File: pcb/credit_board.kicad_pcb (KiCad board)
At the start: 2 copper layers, 17 parts, among them J1 amp or pull-up, J2 amp or pull-up, J3 Jack-DC, J4 amp or pull-up, J5 clk, J6 clk, U1 74HC04, Y1 10MHz, Y2 32.768 kHz

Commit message: beta ground にした。
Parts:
- moved J3 9.24 mm to (171.8, 105.4)
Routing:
- net GND: track 60.3 -> 0.00 mm, vias 2 -> 0
- net VCC: track 73.6 -> 81.6 mm
- net Net-(J2-Pad3): track 5.08 -> 2.54 mm
- added copper zone on B.Cu, net GND
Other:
- board outline added: 45.7 x 41.9 mm
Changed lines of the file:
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@@
     (links 31)
     (no_connects 0)
-    (area 138.725 98.684999 181.535001 136.690002)
+    (area 139.624999 96.444999 185.495001 138.505001)
     (thickness 1.6)
-    (drawings 0)
-    (tracks 63)
+    (drawings 4)
+    (tracks 52)
     (zones 0)
     (modules 17)
@@
   )
   (module Connectors:Barrel_Jack_CUI_PJ-102AH (layer F.Cu)
-    (at 162.56 105.41 90)
+    (at 171.8 105.41 90)
     (descr "Thin-pin DC Barrel Jack, https://cdn-shop.adafruit.com/datasheets/21mmdcjackDatasheet.pdf")
     (tags "Power Jack")
@@
     )
   )
+  (gr_line (start 185.42 138.43) (end 185.42 96.52) (layer Edge.Cuts) (width 0.15))
+  (gr_line (start 139.7 138.43) (end 185.42 138.43) (layer Edge.Cuts) (width 0.15))
+  (gr_line (start 139.7 96.52) (end 139.7 138.43) (layer Edge.Cuts) (width 0.15))
+  (gr_line (start 185.42 96.52) (end 139.7 96.52) (layer Edge.Cuts) (width 0.15))
   (segment (start 172.72 115.57) (end 170.18 115.57) (width 0.25) (layer B.Cu) (net 1))
   (segment (start 175.26 115.57) (end 172.72 115.57) (width 0.25) (layer B.Cu) (net 1))
@@
   (segment (start 170.18 115.57) (end 167.64 115.57) (width 0.25) (layer B.Cu) (net 1))
   (segment (start 162.74 115.75) (end 162.56 115.57) (width 0.25) (layer B.Cu) (net 1))
-  (segment (start 180.26 115.57) (end 180.26 112.95) (width 0.25) (layer B.Cu) (net 2))
-  (segment (start 180.26 112.95) (end 172.72 105.41) (width 0.25) (layer B.Cu) (net 2))
-  (segment (start 180.26 115.57) (end 180.26 120.65) (width 0.25) (layer B.Cu) (net 2))
-  (segment (start 168.56 105.41) (end 172.72 105.41) (width 0.25) (layer B.Cu) (net 2))
-  (segment (start 167.64 135.89) (end 180.26 123.27) (width 0.25) (layer B.Cu) (net 2))
-  (segment (start 180.26 120.65) (end 180.26 123.27) (width 0.25) (layer B.Cu) (net 2))
-  (via (at 157.48 130.81) (size 0.6) (drill 0.4) (layers F.Cu B.Cu) (net 2))
-  (segment (start 157.48 133.35) (end 157.48 130.81) (width 0.25) (layer F.Cu) (net 2))
-  (segment (start 160.02 135.89) (end 157.48 133.35) (width 0.25) (layer F.Cu) (net 2))
-  (via (at 160.02 135.89) (size 0.6) (drill 0.4) (layers F.Cu B.Cu) (net 2))
-  (segment (start 154.94 128.27) (end 157.48 130.81) (width 0.25) (layer B.Cu) (net 2))
-  (segment (start 160.02 135.89) (end 167.64 135.89) (width 0.25) (layer B.Cu) (net 2))
   (segment (start 175.26 120.65) (end 174.134999 119.524999) (width 0.25) (layer B.Cu) (net 3))
   (segment (start 172.72 118.11) (end 175.26 120.65) (width 0.25) (layer B.Cu) (net 3))
@@
   (segment (start 165.1 125.73) (end 172.72 125.73) (width 0.25) (layer B.Cu) (net 8))
   (segment (start 165.1 125.73) (end 162.56 125.73) (width 0.25) (layer B.Cu) (net 8))
-  (segment (start 172.72 128.27) (end 167.64 128.27) (width 0.25) (layer B.Cu) (net 9))
+  (segment (start 172.72 128.27) (end 170.18 128.27) (width 0.25) (layer B.Cu) (net 9))
   (segment (start 152.4 115.57) (end 154.94 115.57) (width 0.25) (layer B.Cu) (net 10))
   (segment (start 149.86 115.57) (end 152.4 115.57) (width 0.25) (layer B.Cu) (net 10))
   (segment (start 152.4 113.03) (end 152.4 110.49) (width 0.25) (layer B.Cu) (net 11))
   (segment (start 154.94 113.03) (end 152.4 113.03) (width 0.25) (layer B.Cu) (net 11))
+  (segment (start 163.83 105.41) (end 171.8 105.41) (width 0.25) (layer B.Cu) (net 12))
+  (segment (start 162.56 106.68) (end 163.83 105.41) (width 0.25) (layer B.Cu) (net 12))
+  (segment (start 162.56 113.03) (end 162.56 106.68) (width 0.25) (layer B.Cu) (net 12))
+  (segment (start 171.8 105.41) (end 171.8 103.71) (width 0.25) (layer B.Cu) (net 12))
+  (segment (start 171.8 103.71) (end 174.8 100.71) (width 0.25) (layer B.Cu) (net 12))
   (segment (start 160.02 133.35) (end 165.1 133.35) (width 0.25) (layer B.Cu) (net 12))
   (segment (start 165.1 133.35) (end 167.64 130.81) (width 0.25) (layer B.Cu) (net 12))
@@
   (segment (start 160.02 130.81) (end 160.02 128.27) (width 0.25) (layer B.Cu) (net 12))
   (segment (start 160.02 115.57) (end 162.56 113.03) (width 0.25) (layer B.Cu) (net 12))
-  (segment (start 162.56 113.03) (end 162.56 105.41) (width 0.25) (layer B.Cu) (net 12))
-  (segment (start 162.56 105.41) (end 162.56 102.87) (width 0.25) (layer B.Cu) (net 12))
-  (segment (start 162.56 102.87) (end 163.4 102.87) (width 0.25) (layer B.Cu) (net 12))
-  (segment (start 163.4 102.87) (end 165.56 100.71) (width 0.25) (layer B.Cu) (net 12))
   (segment (start 152.4 120.65) (end 154.94 120.65) (width 0.25) (layer B.Cu) (net 13))
   (segment (start 162.56 130.81) (end 162.56 128.27) (width 0.25) (layer B.Cu) (net 14))
@@
   (segment (start 152.4 123.19) (end 154.94 123.19) (width 0.25) (layer B.Cu) (net 16))
   (segment (start 149.86 125.73) (end 152.4 125.73) (width 0.25) (layer B.Cu) (net 17))
+  (zone (net 2) (net_name GND) (layer B.Cu) (hatch edge 0.508)
+    (connect_pads (clearance 0.508))
+    (min_thickness 0.254)
+    (fill yes (arc_segments 16) (thermal_gap 0.508) (thermal_bridge_width 0.508))
+    (polygon
+      (pts
+        (xy 185.42 97.79) (xy 185.42 137.16) (xy 139.7 137.16) (xy 139.7 97.79)
+      )
+    )
+  )
 )

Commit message: board の clock 部は完成。
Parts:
- J1: value amp or pull-up -> Jack-DC; footprint Pin_Headers:Pin_Header_Straight_1x03_Pitch2.54mm -> Connectors:Barrel_Jack_CUI_PJ-102AH
- J3: value Jack-DC -> amp or pull-up; footprint Connectors:Barrel_Jack_CUI_PJ-102AH -> Pin_Headers:Pin_Header_Straight_1x03_Pitch2.54mm
- J5, J6: footprint Pin_Headers:Pin_Header_Straight_1x01_Pitch2.54mm -> Connectors:Pin_d1.0mm_L10.0mm
- R1: value 1MΩ -> 10MΩ
- R2: value 10MΩ -> 1MΩ
- moved C2 46.0 mm to (134.6, 99.1), turned to 180 degrees
- moved C1 45.4 mm to (134.6, 95.2), turned to 180 degrees
- moved R5 35.6 mm to (141.0, 108.0)
- moved Y1 34.7 mm to (139.7, 95.2)
- moved R4 30.7 mm to (171.4, 105.4), turned to 0 degrees
- moved J3 27.1 mm to (144.8, 102.9), turned to 0 degrees
- moved J2 23.4 mm to (167.6, 100.3)
- moved R1 21.8 mm to (160.0, 100.3)
- moved J5 21.6 mm to (148.6, 114.3), turned to 0 degrees
- moved R6 20.7 mm to (163.8, 110.5), turned to 0 degrees
- moved R3 20.7 mm to (163.8, 100.3)
- moved Y2 19.3 mm to (160.0, 92.7), turned to 0 degrees
- moved R2 19.3 mm to (144.8, 97.8)
- moved U1 18.9 mm to (148.6, 95.2)
- moved J4 17.0 mm to (160.0, 105.4)
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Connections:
- net Net-(J4-Pad3) renamed /pull-up2
- J1 pad 1: Net-(J1-Pad1) -> VCC
- J1 pad 2: Net-(J1-Pad2) -> GND
- J1 pad 3: Net-(J1-Pad3) -> VCC
- J2 pad 1: Net-(J2-Pad1) -> /output1
- J2 pad 2: Net-(J2-Pad2) -> /amp1
- J2 pad 3: Net-(J2-Pad3) -> /pull-up1
- J3 pad 1: VCC -> /amp3
- J3 pad 2: GND -> Net-(J3-Pad2)
- J3 pad 3: VCC -> /pull-up3
- J4 pad 1: Net-(J4-Pad1) -> /amp2
- J5 pad 1: Net-(J5-Pad1) -> /output3
- J6 pad 1: Net-(J6-Pad1) -> /output2
- R1 pad 1: Net-(C2-Pad1) -> Net-(R1-Pad1)
- R1 pad 2: Net-(C1-Pad1) -> Net-(R1-Pad2)
- R2 pad 1: Net-(R2-Pad1) -> Net-(C2-Pad1)
- R2 pad 2: Net-(R2-Pad2) -> Net-(C1-Pad1)
- R3 pad 1: Net-(R2-Pad1) -> Net-(R1-Pad1)
- R3 pad 2: Net-(J1-Pad1) -> /output1
- R4 pad 1: Net-(J1-Pad3) -> /pull-up1
- R5 pad 1: Net-(J2-Pad3) -> /pull-up3
- U1 pad 1: Net-(R2-Pad2) -> Net-(C1-Pad1)
- U1 pad 10: Net-(J2-Pad1) -> /amp2
- U1 pad 11: Net-(C2-Pad1) -> /amp1
- U1 pad 12: Net-(C2-Pad1) -> Net-(R1-Pad1)
- U1 pad 13: Net-(C1-Pad1) -> Net-(R1-Pad2)
- U1 pad 2: Net-(R2-Pad1) -> Net-(C2-Pad1)
- U1 pad 3: Net-(J1-Pad2) -> Net-(C2-Pad1)
- U1 pad 4: Net-(J4-Pad1) -> /amp3
- U1 pad 5: Net-(J4-Pad2) -> Net-(J3-Pad2)
- U1 pad 6: Net-(J6-Pad1) -> /output3
- U1 pad 8: Net-(J5-Pad1) -> /output2
- U1 pad 9: Net-(J2-Pad2) -> Net-(J4-Pad2)
- Y2 pad 1: Net-(R2-Pad2) -> Net-(R1-Pad2)
- Y2 pad 2: Net-(J1-Pad1) -> /output1
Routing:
- net /amp1: track 0.00 -> 11.4 mm
- net /output1: track 0.00 -> 11.1 mm
- net Net-(J2-Pad2): track 10.2 -> 0.00 mm
- net Net-(J2-Pad1): track 10.2 -> 0.00 mm
- net /output3: track 0.00 -> 9.94 mm
- net Net-(R1-Pad2): track 0.00 -> 8.89 mm
- net Net-(R1-Pad1): track 0.00 -> 7.62 mm
- net Net-(J1-Pad2): track 7.62 -> 0.00 mm
- net Net-(J6-Pad1): track 7.18 -> 0.00 mm
- net Net-(J1-Pad1): track 6.13 -> 0.00 mm
- net Net-(R2-Pad2): track 5.08 -> 0.00 mm
- net Net-(R2-Pad1): track 5.08 -> 0.00 mm
- net Net-(J3-Pad2): track 0.00 -> 3.81 mm
- net /pull-up3: track 0.00 -> 3.81 mm
- net /pull-up1: track 0.00 -> 3.81 mm
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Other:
- board size 45.7 x 41.9 mm -> 53.3 x 35.6 mm

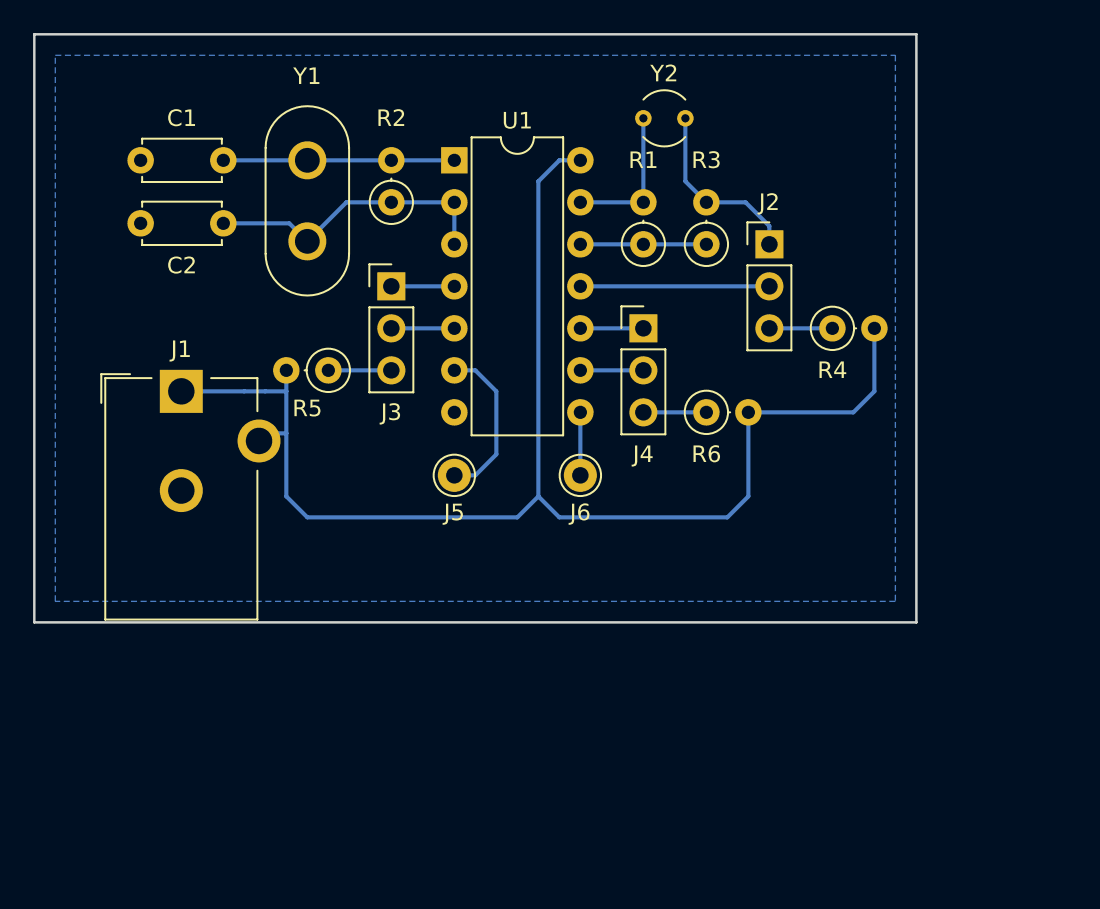
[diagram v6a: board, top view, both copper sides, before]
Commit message: U1 GND, J1 GND の接続にViaを使用した。
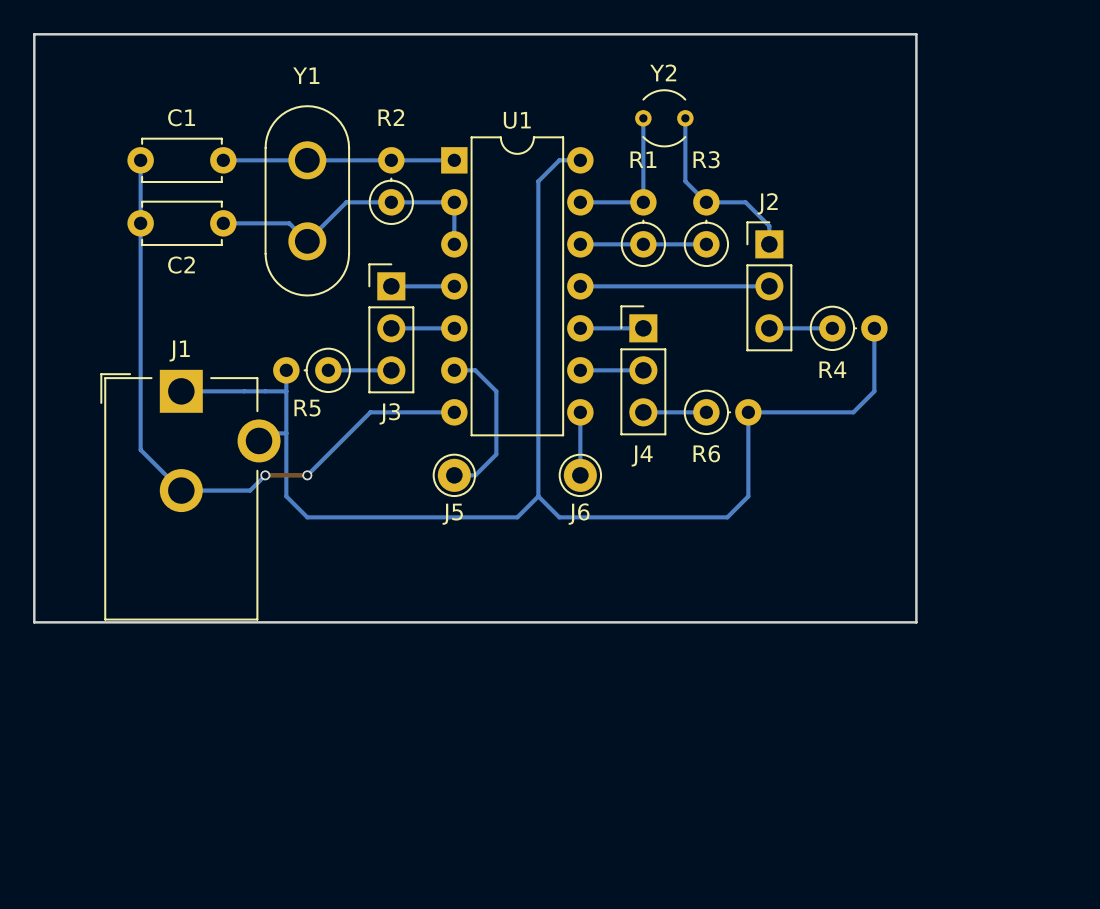
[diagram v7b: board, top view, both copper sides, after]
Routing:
- net GND: track 0.00 -> 39.5 mm, vias 0 -> 2
- removed copper zone on B.Cu, net GND
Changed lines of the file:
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@@
   (general
     (links 31)
-    (no_connects 23)
-    (area 123.114999 87.554999 176.605001 123.265001)
+    (no_connects 0)
+    (area 123.114999 87.554999 176.605001 123.645001)
     (thickness 1.6)
     (drawings 4)
-    (tracks 53)
+    (tracks 63)
     (zones 0)
     (modules 17)
@@
   (layers
     (0 F.Cu signal)
-    (31 B.Cu signal hide)
+    (31 B.Cu signal)
     (32 B.Adhes user)
     (33 F.Adhes user)
@@
   (segment (start 139.7 95.25) (end 144.78 95.25) (width 0.25) (layer B.Cu) (net 1))
   (segment (start 144.78 95.25) (end 148.59 95.25) (width 0.25) (layer B.Cu) (net 1))
+  (segment (start 136.24 115.22) (end 137.16 114.3) (width 0.25) (layer B.Cu) (net 2))
+  (segment (start 132.08 115.22) (end 136.24 115.22) (width 0.25) (layer B.Cu) (net 2))
+  (via (at 137.16 114.3) (size 0.6) (drill 0.4) (layers F.Cu B.Cu) (net 2))
+  (segment (start 139.7 114.3) (end 137.16 114.3) (width 0.25) (layer F.Cu) (net 2))
+  (segment (start 143.51 110.49) (end 139.7 114.3) (width 0.25) (layer B.Cu) (net 2))
+  (via (at 139.7 114.3) (size 0.6) (drill 0.4) (layers F.Cu B.Cu) (net 2))
+  (segment (start 148.59 110.49) (end 143.51 110.49) (width 0.25) (layer B.Cu) (net 2))
+  (segment (start 129.62 99.06) (end 129.62 112.76) (width 0.25) (layer B.Cu) (net 2))
+  (segment (start 129.62 112.76) (end 132.08 115.22) (width 0.25) (layer B.Cu) (net 2))
+  (segment (start 129.62 95.25) (end 129.62 99.06) (width 0.25) (layer B.Cu) (net 2))
   (segment (start 134.62 99.06) (end 138.61 99.06) (width 0.25) (layer B.Cu) (net 3))
   (segment (start 138.61 99.06) (end 139.7 100.15) (width 0.25) (layer B.Cu) (net 3))
@@
   (segment (start 160.02 97.79) (end 160.02 92.71) (width 0.25) (layer B.Cu) (net 17))
   (segment (start 156.21 97.79) (end 160.02 97.79) (width 0.25) (layer B.Cu) (net 17))
-  (zone (net 2) (net_name GND) (layer B.Cu) (hatch edge 0.508)
-    (connect_pads (clearance 0.508))
-    (min_thickness 0.254)
-    (fill yes (arc_segments 16) (thermal_gap 0.508) (thermal_bridge_width 0.508))
-    (polygon
-      (pts
-        (xy 175.26 90.17) (xy 175.26 121.92) (xy 124.46 121.92) (xy 124.46 88.9) (xy 175.26 88.9)
-      )
-    )
-  )
 )
